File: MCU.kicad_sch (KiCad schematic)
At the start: 9 parts, among them J200 LORA, J201 GPS, J202 ANEM, J203 MICROSD, U200 BP, U201 BNO085

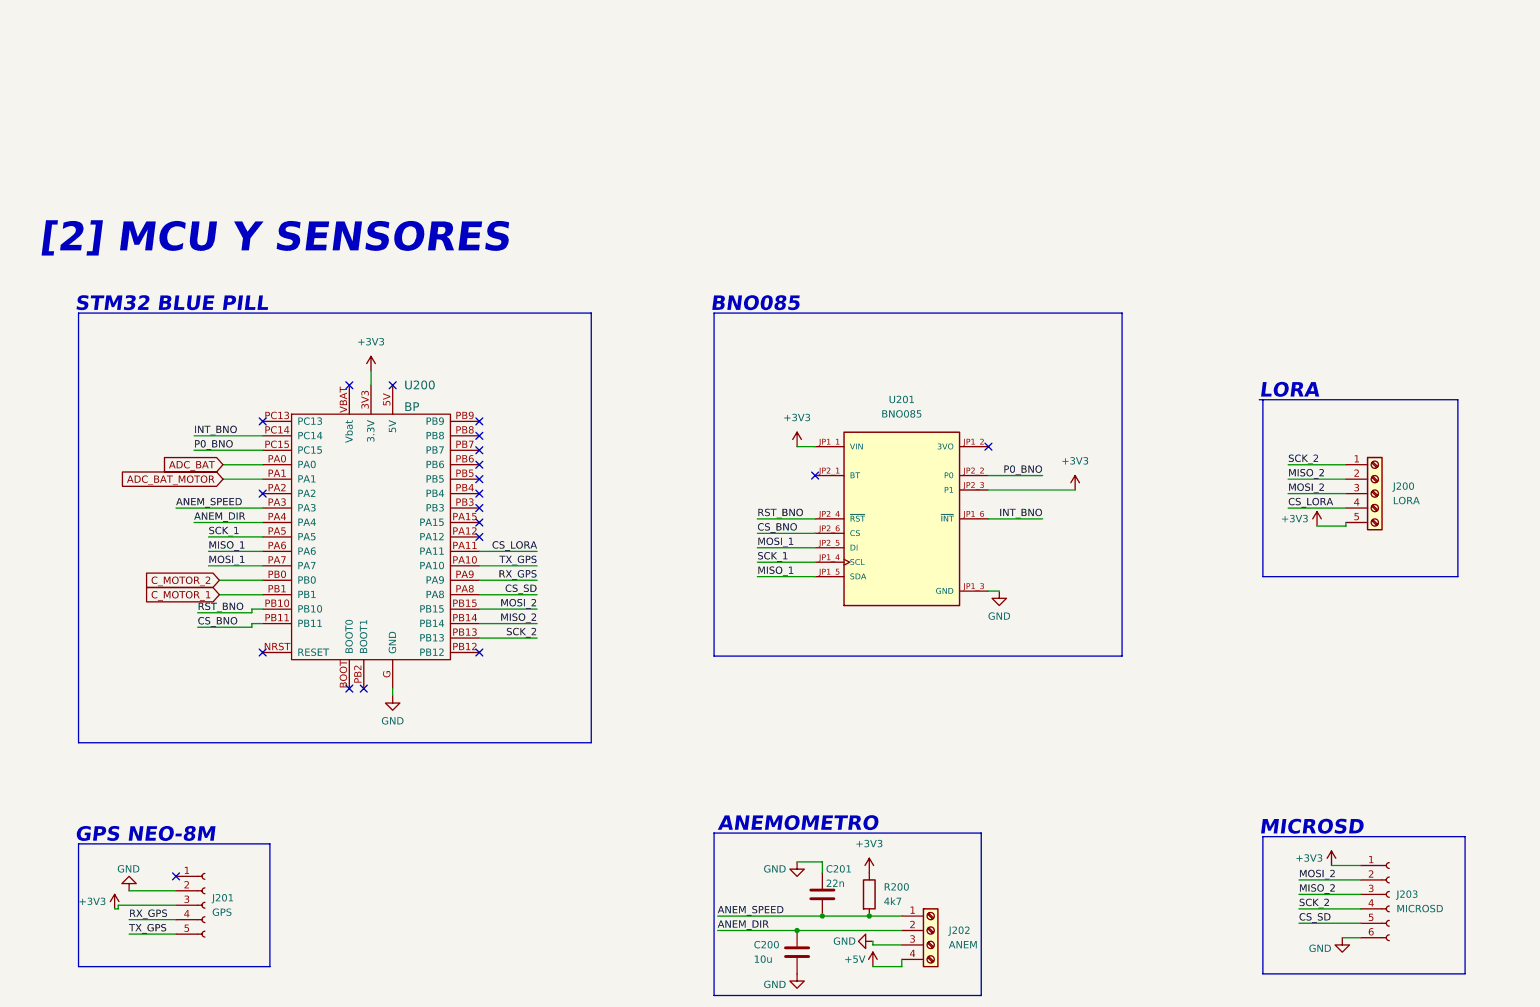
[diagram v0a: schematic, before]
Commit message: Cambios: Lora comunicacion UART, comunicacion I2C para analizer y Atmega
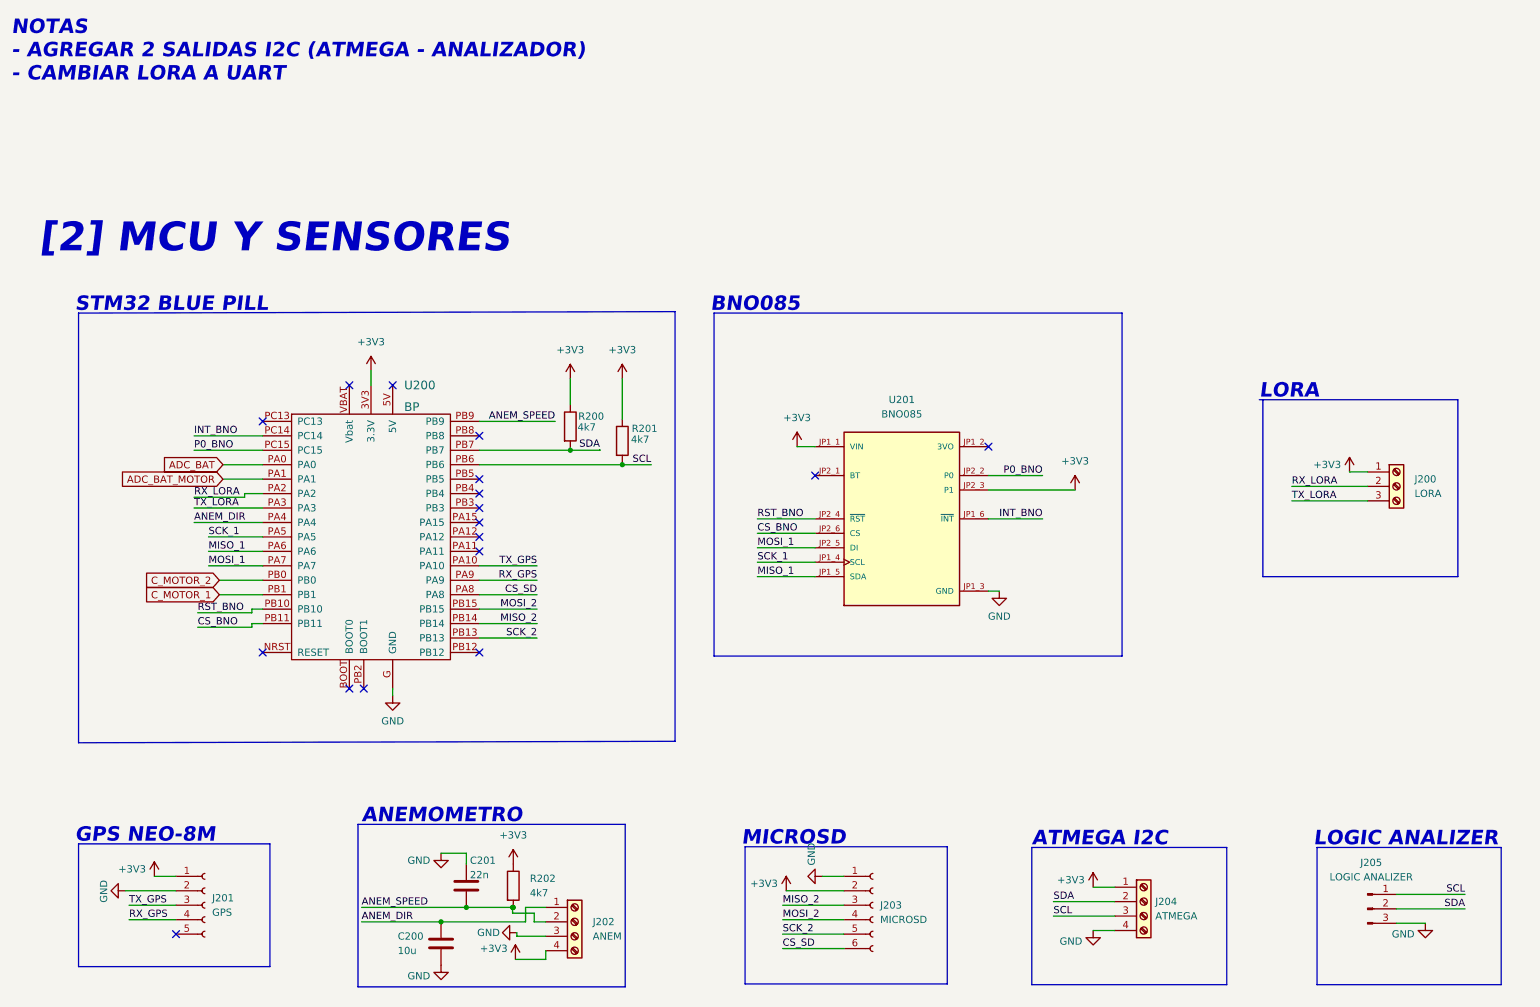
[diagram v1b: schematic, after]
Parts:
- removed J200: LORA, Connector_Phoenix_MSTB:PhoenixContact_MSTBA_2,5_5-G-5,08_1x05_P5.08mm_Horizontal, symbol Connector:Screw_Terminal_01x05
- added J200: LORA, Connector_Phoenix_MSTB:PhoenixContact_MSTBA_2,5_3-G-5,08_1x03_P5.08mm_Horizontal, symbol Connector:Screw_Terminal_01x03
- added J204: ATMEGA, Connector_Phoenix_MSTB:PhoenixContact_MSTBA_2,5_4-G-5,08_1x04_P5.08mm_Horizontal, symbol Connector:Screw_Terminal_01x04
- added J205: LOGIC ANALIZER, Connector_PinHeader_2.54mm:PinHeader_1x03_P2.54mm_Vertical, symbol Connector:Conn_01x03_Male
- added R200, R201: 4k7, Resistor_THT:R_Axial_DIN0204_L3.6mm_D1.6mm_P5.08mm_Horizontal, symbol Device:R
- renumbered R200 to R202
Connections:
- net +5V is gone; now on net +3V3: J202.4 (Pin_4)
- net +3V3: now also J201.1 (Pin_1), J203.2 (Pin_2), J200.1 (Pin_1), J204.1 (Pin_1), R200.1, R201.1; no longer J201.3 (Pin_3), J203.1 (Pin_1)
- net ANEM_DIR: now also J202.1 (Pin_1); no longer J202.2 (Pin_2)
- net ANEM_SPEED: now also J202.2 (Pin_2), U200.PB9; no longer J202.1 (Pin_1), U200.PA3
- net CS_SD: now also J203.6 (Pin_6); no longer J203.5 (Pin_5)
- net GND: now also J203.1 (Pin_1), J204.4 (Pin_4), J205.3 (Pin_3); no longer J203.6 (Pin_6)
- net MOSI_2: now also J203.4 (Pin_4); no longer J203.2 (Pin_2)
- net SCK_2: now also J203.5 (Pin_5); no longer J203.4 (Pin_4)
- net TX_GPS: now also J201.3 (Pin_3); no longer J201.5 (Pin_5)
- net RX_LORA: now reaches U200.PA2
- net RX_LORA: now also J200.2 (Pin_2)
- net SCL: now reaches U200.PB6
- net SCL: now also J204.3 (Pin_3), J205.1 (Pin_1), R201.2
- net SDA: now reaches U200.PB7
- net SDA: now also J204.2 (Pin_2), J205.2 (Pin_2), R200.2
- net CS_LORA: no longer names the net of U200.PA11
- new net TX_LORA: J200.3 (Pin_3), U200.PA3
- no-connect marks 20 -> 17
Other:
- note added: "ATMEGA I2C"
- note added: "LOGIC ANALIZER"
- note added: "NOTAS - AGREGAR 2 SALIDAS I2C (ATMEGA - ANALIZADOR) - CAMBIAR LORA A UART"
- moved on the sheet: C200, C201, J202, J203, R202
